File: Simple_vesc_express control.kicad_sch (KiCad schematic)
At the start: 38 parts, among them J1 Conn_01x04, J10 Conn_01x06, J2 Conn_01x04, J4 USB_C_Receptacle_USB2.0, J5 Conn_01x03, J6 Conn_01x03, J7 Conn_01x03, J8 Conn_01x02, J9 Conn_01x04, Q1 NMOS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

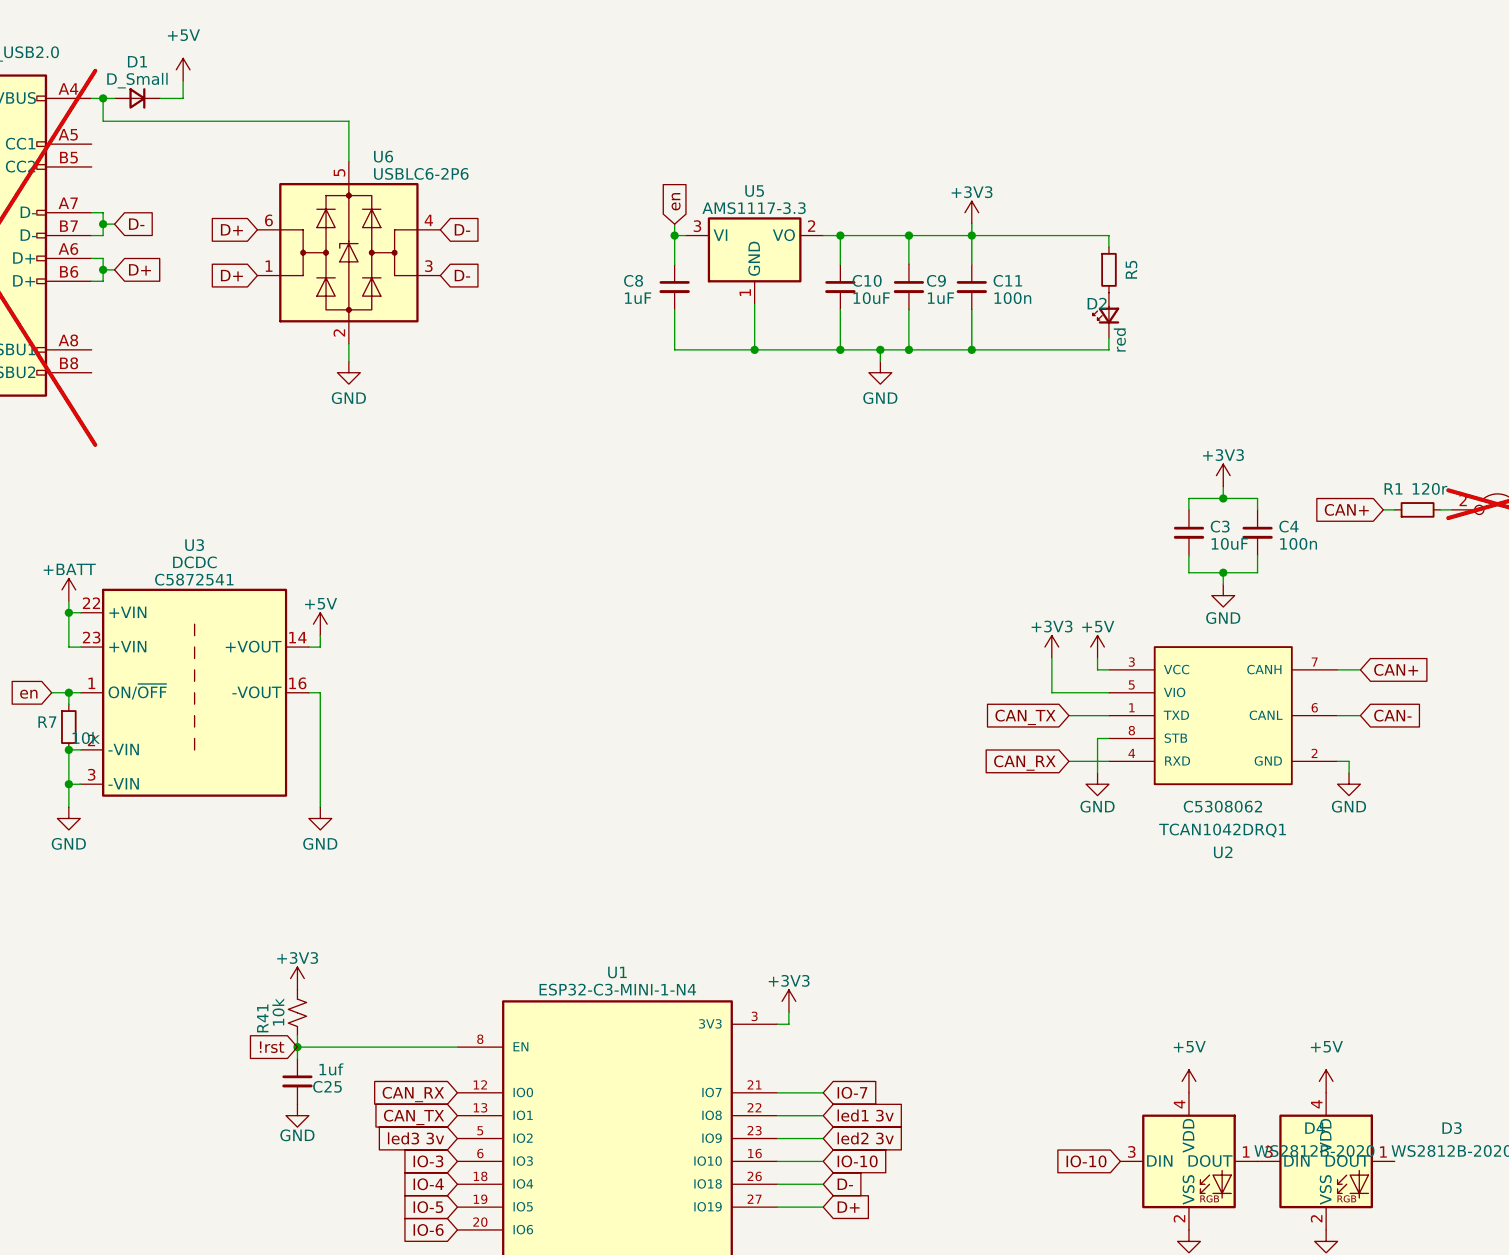
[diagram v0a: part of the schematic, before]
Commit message: changed usb powered parts
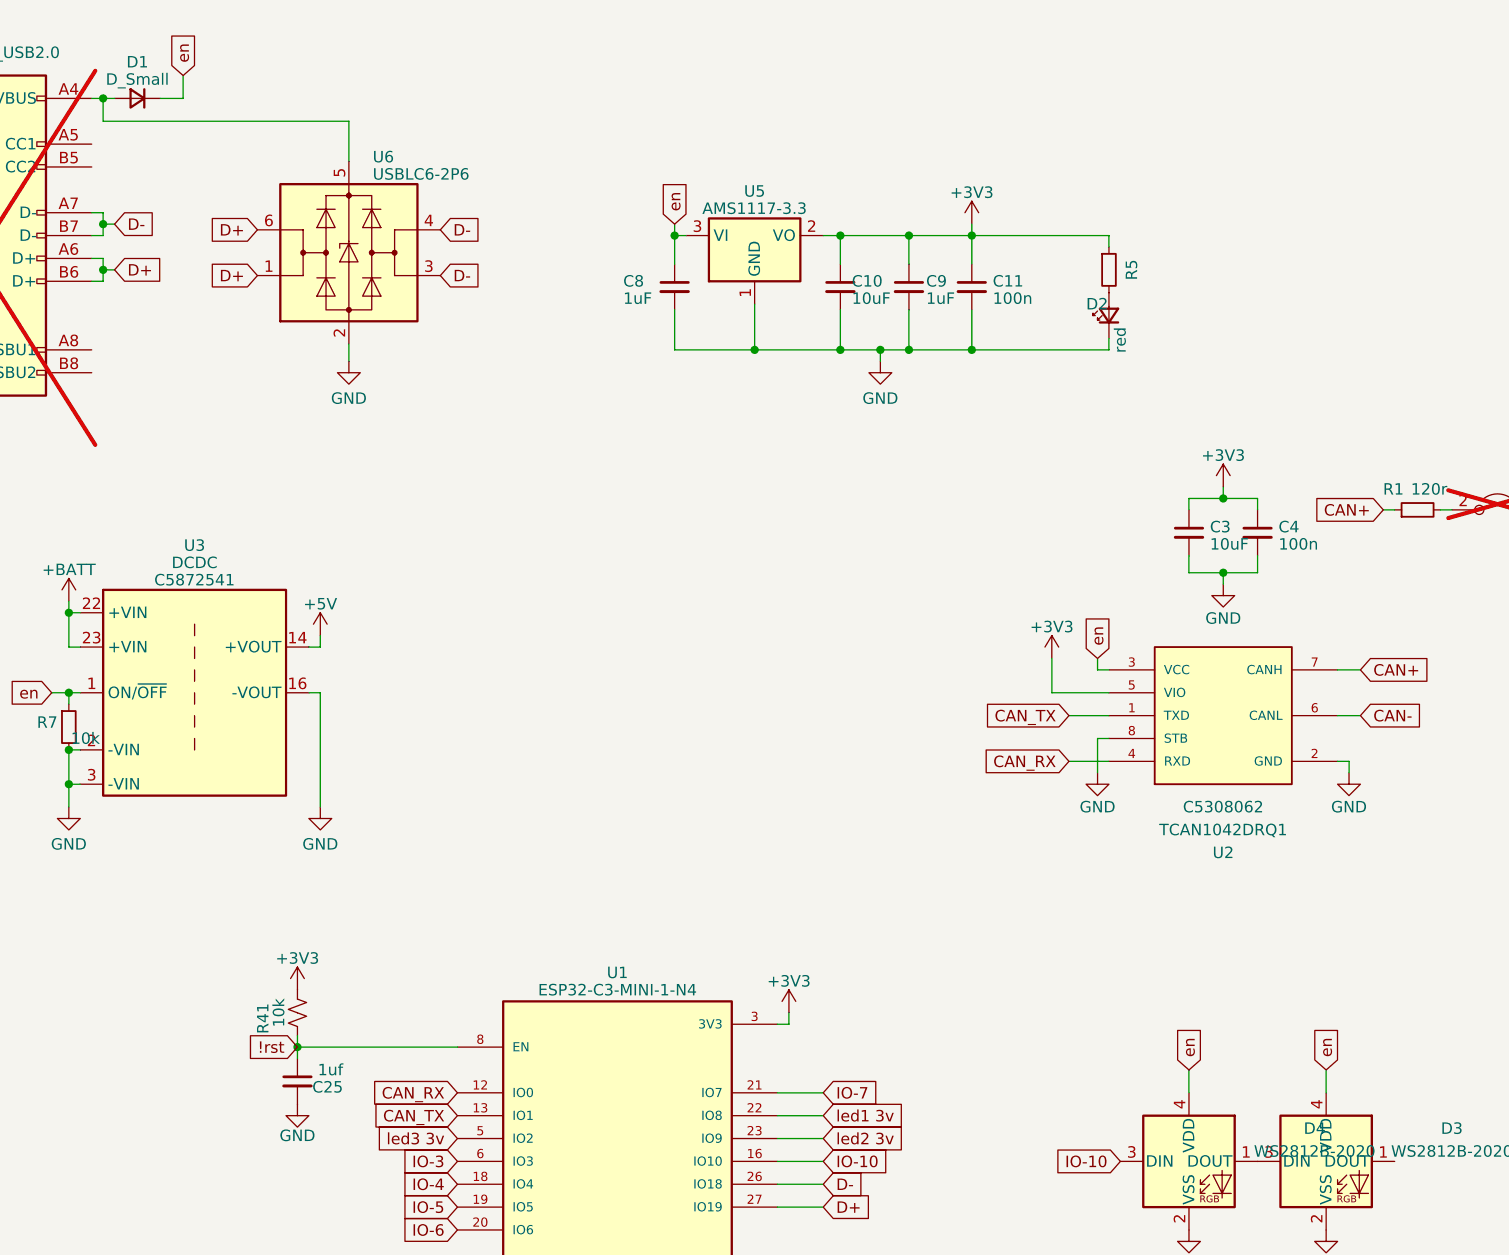
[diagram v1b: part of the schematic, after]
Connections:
- net +5V: no longer D1.1 (K), D3.4 (VDD), D4.4 (VDD), U2.3 (VCC)
- net en: now also D1.1 (K), D3.4 (VDD), D4.4 (VDD), U2.3 (VCC)
